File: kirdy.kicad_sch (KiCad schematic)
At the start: 0 parts

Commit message: add PoE
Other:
- added sheet digital supply (dsupply.kicad_sch)

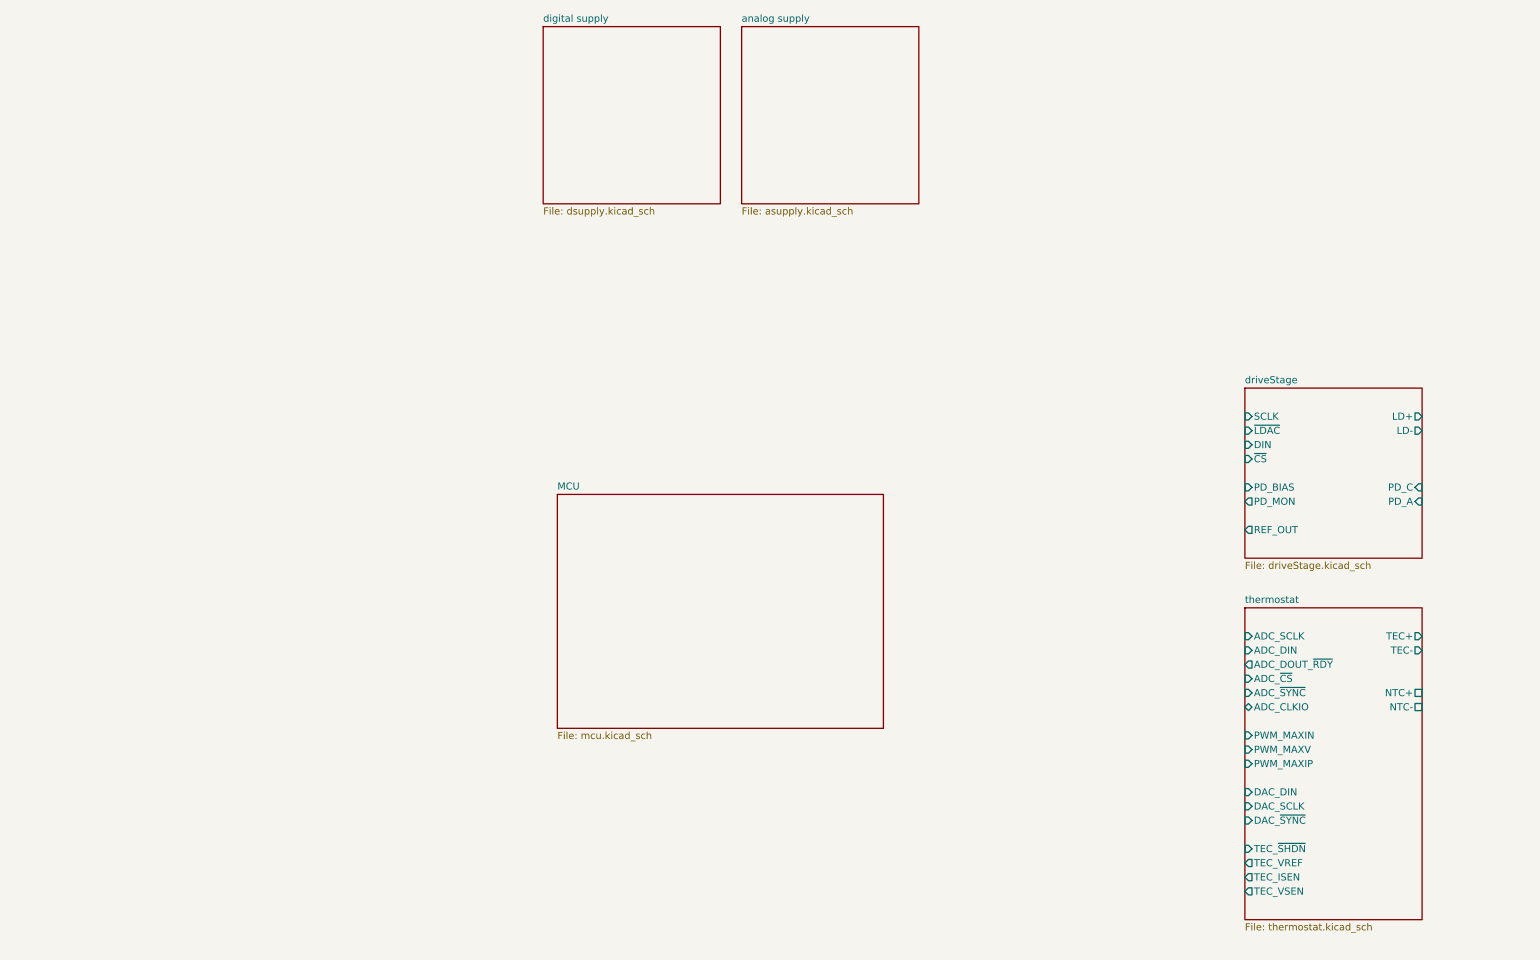
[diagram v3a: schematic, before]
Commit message: add ethernet
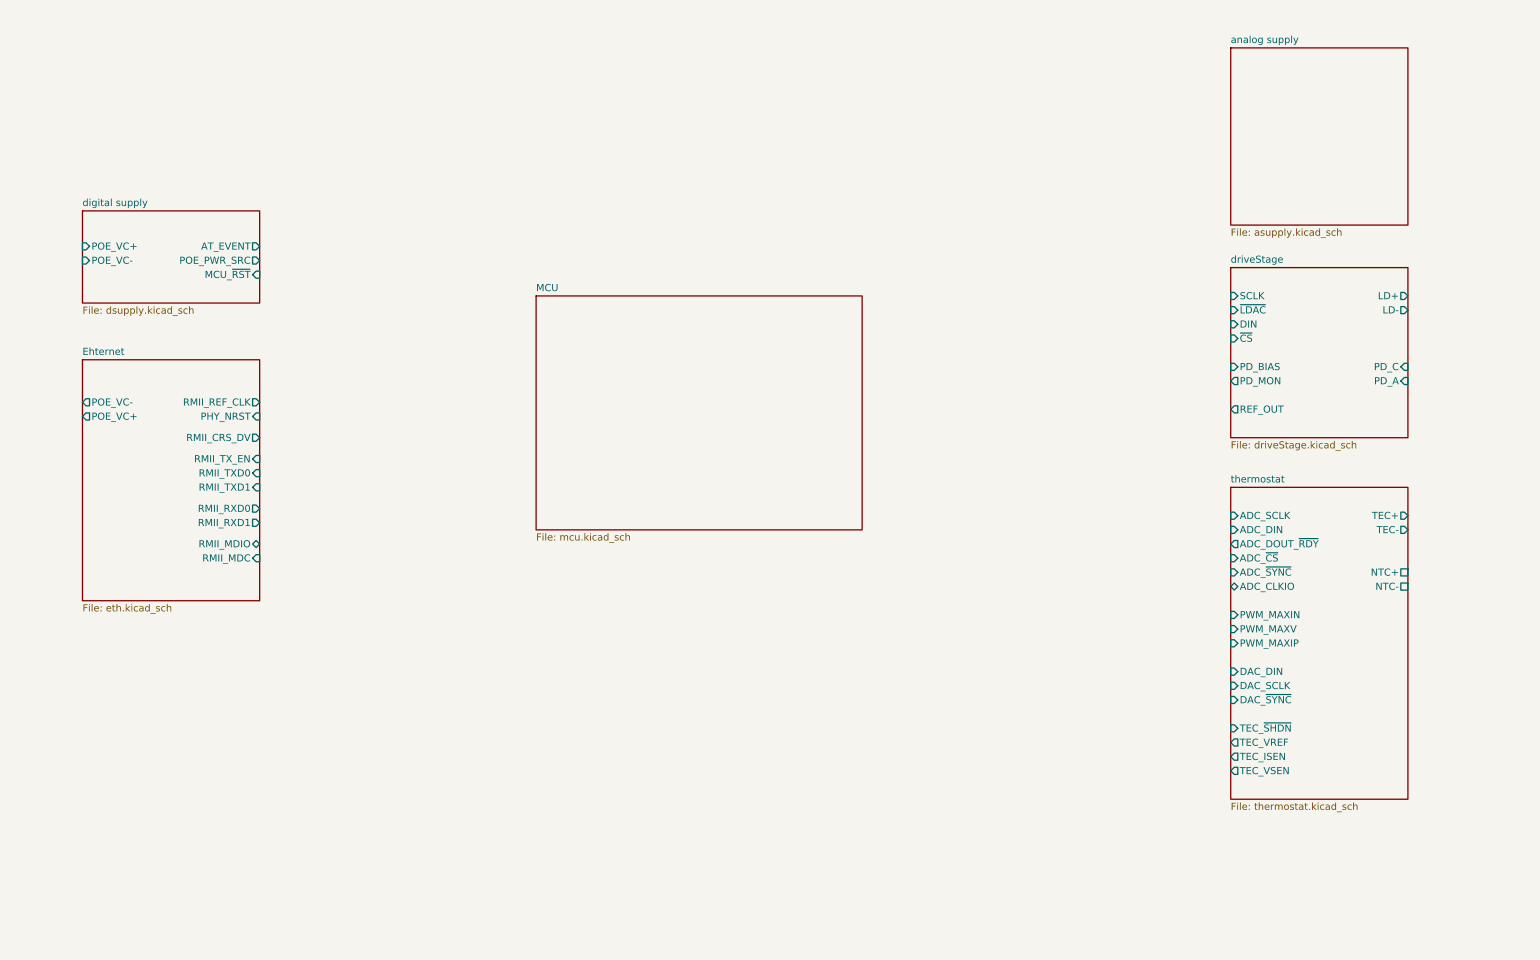
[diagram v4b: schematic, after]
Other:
- added sheet Ehternet (eth.kicad_sch)
- sheet digital supply ports: added AT_EVENT, MCU_~{RST}, POE_PWR_SRC, POE_VC+, POE_VC-; removed none

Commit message: add USB
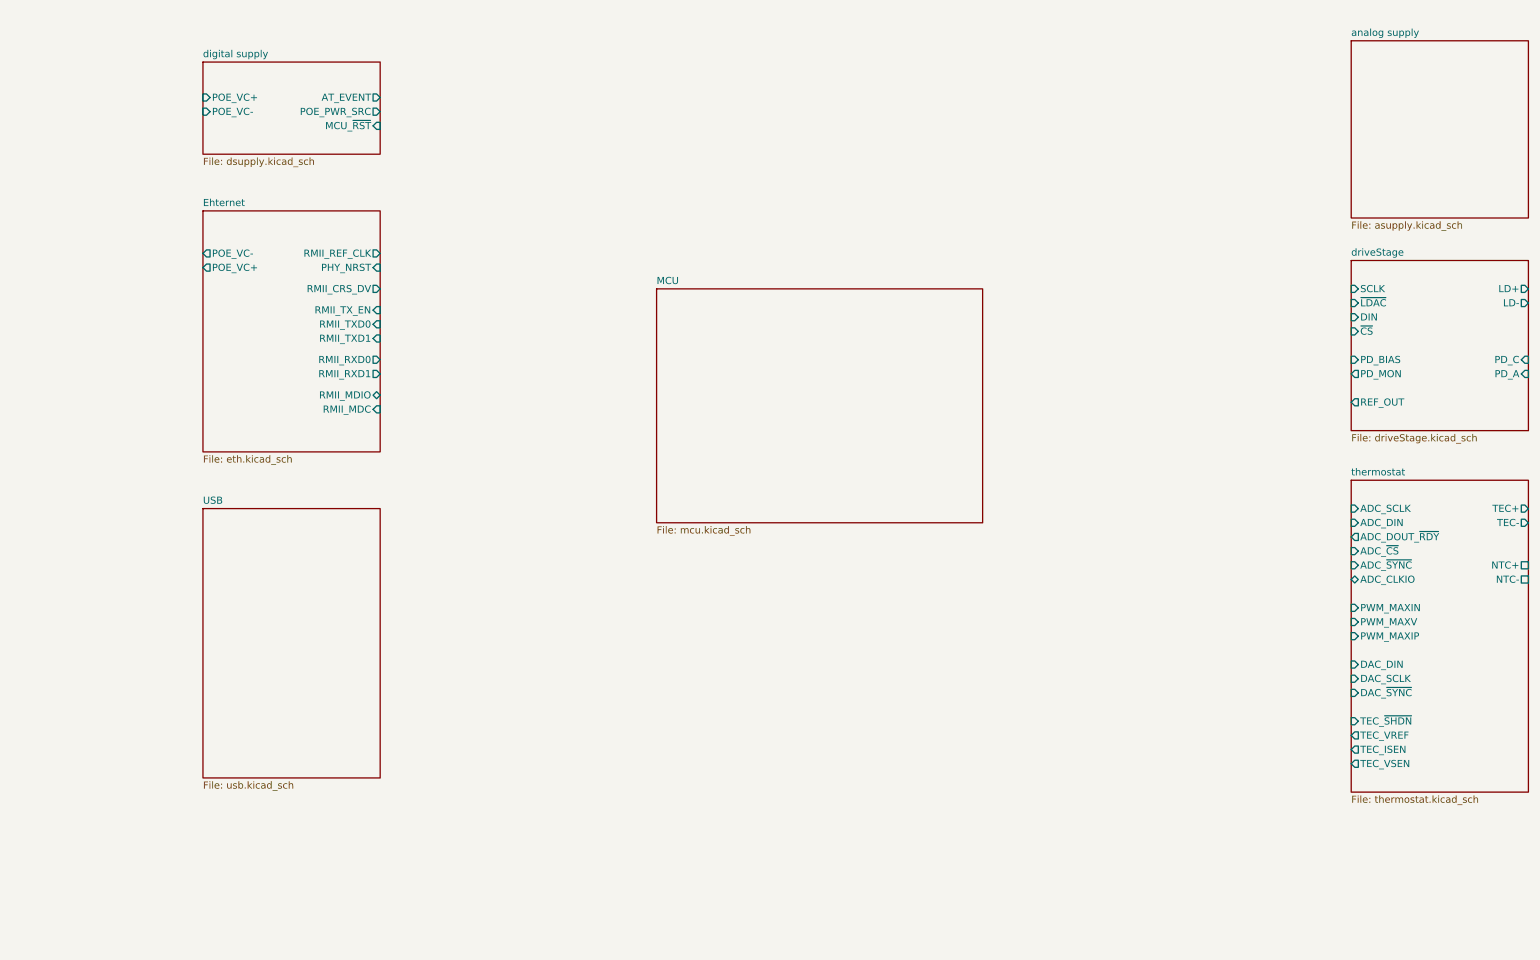
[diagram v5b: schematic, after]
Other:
- added sheet USB (usb.kicad_sch)
- company: (none) -> M-Labs
- title: (none) -> Kirdy

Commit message: add MCU basic connections
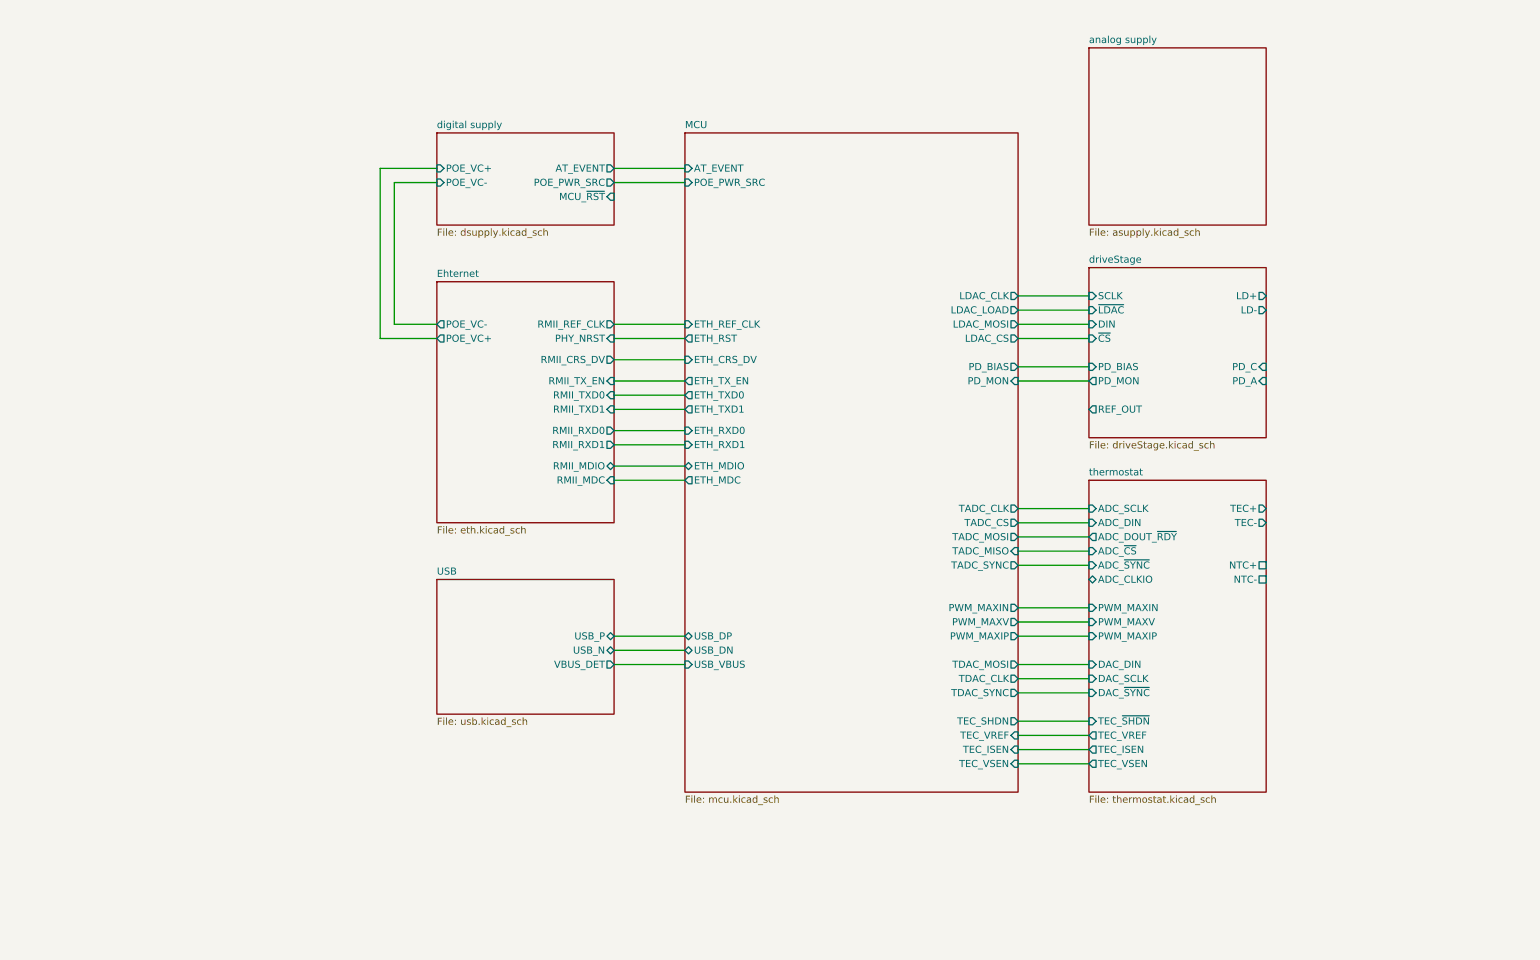
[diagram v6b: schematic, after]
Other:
- sheet MCU ports: added AT_EVENT, ETH_CRS_DV, ETH_MDC, ETH_MDIO, ETH_REF_CLK, ETH_RST, ETH_RXD0, ETH_RXD1, ETH_TXD0, ETH_TXD1, ETH_TX_EN, LDAC_CLK, LDAC_CS, LDAC_LOAD, LDAC_MOSI, PD_BIAS, PD_MON, POE_PWR_SRC, PWM_MAXIN, PWM_MAXIP, PWM_MAXV, TADC_CLK, TADC_CS, TADC_MISO, TADC_MOSI, TADC_SYNC, TDAC_CLK, TDAC_MOSI, TDAC_SYNC, TEC_ISEN, TEC_SHDN, TEC_VREF, TEC_VSEN, USB_DN, USB_DP, USB_VBUS; removed none
- sheet USB ports: added USB_N, USB_P, VBUS_DET; removed none

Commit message: complete mcu
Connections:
- no-connect marks 0 -> 1
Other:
- sheet MCU ports: added MCU_RSTn; removed none
- sheet driveStage ports: added none; removed REF_OUT

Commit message: first draft complete
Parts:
- added J8, J9: Conn_02x05_Odd_Even, symbol Connector_Generic:Conn_02x05_Odd_Even
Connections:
- net driveStage/LD+: now also J8.1 (Pin_1)
- net driveStage/LD-: now also J8.3 (Pin_3)
- net driveStage/PD_A: now also J8.9 (Pin_9)
- net driveStage/PD_C: now also J8.7 (Pin_7)
- net thermostat/NTC+: now also J9.7 (Pin_7)
- net thermostat/NTC-: now also J9.9 (Pin_9)
- net thermostat/TEC+: now also J9.1 (Pin_1)
- net thermostat/TEC-: now also J9.3 (Pin_3)
- new net GND: J8.10 (Pin_10), J8.2 (Pin_2), J8.4 (Pin_4), J8.5 (Pin_5), J8.6 (Pin_6), J8.8 (Pin_8), J9.10 (Pin_10), J9.2 (Pin_2), J9.4 (Pin_4), J9.5 (Pin_5), J9.6 (Pin_6), J9.8 (Pin_8)
- no-connect marks 1 -> 0
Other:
- sheet thermostat ports: added none; removed ADC_CLKIO
